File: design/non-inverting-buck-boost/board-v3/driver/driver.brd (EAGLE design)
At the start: 54.3 x 44.4 mm, 11 parts, among them IC1 L7812, IC2 78L05, T1 BC547

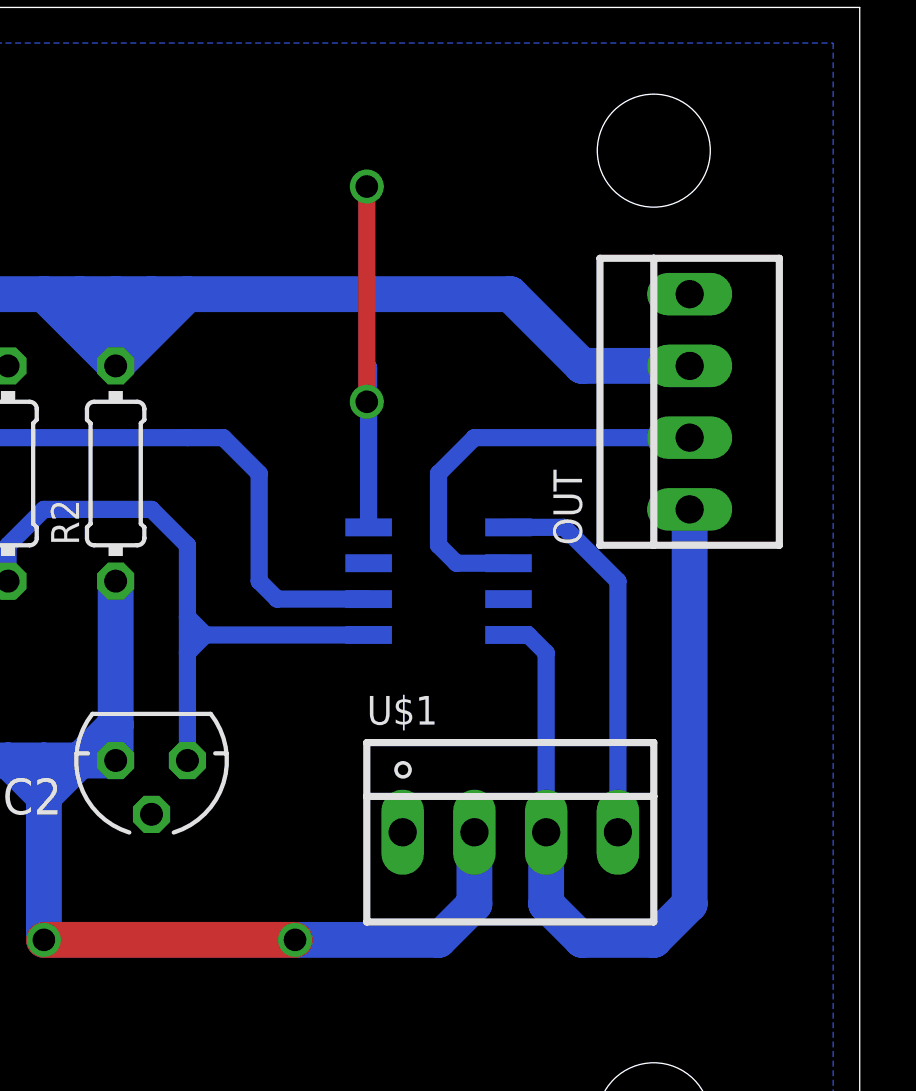
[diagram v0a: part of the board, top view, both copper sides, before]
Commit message: fixed ADuM3220 pins
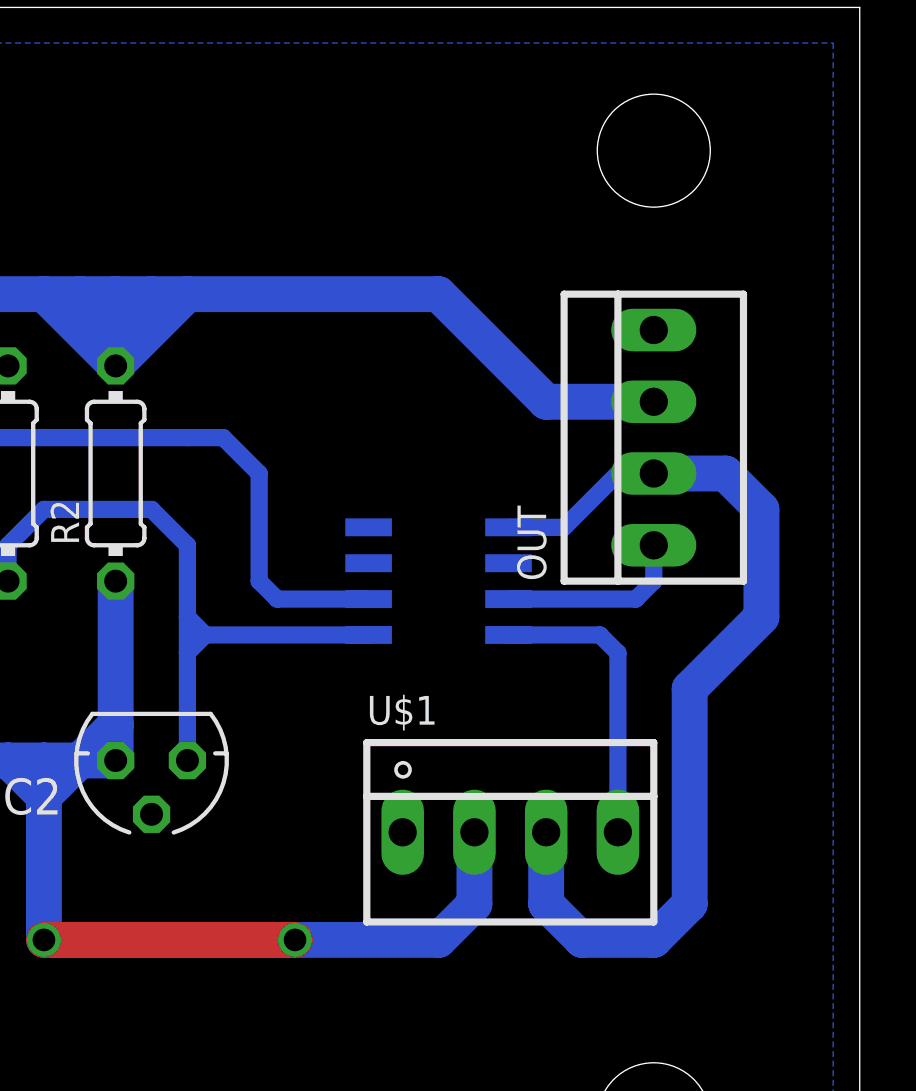
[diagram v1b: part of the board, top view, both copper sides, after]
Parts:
- moved OUT 1.80 mm to (47.0, 29.2)
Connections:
- net VDD2: now also U$2.8; no longer U$2.5
- net VG1: now also OUT.1, U$2.7; no longer OUT.2, U$2.6
- net VS1: now also OUT.2, U$2.5; no longer OUT.1, U$2.8
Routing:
- net GND: track 14.5 -> 0.00 mm, vias 2 -> 0
- net VG1: track 14.7 -> 6.68 mm
- net VS1: track 30.6 -> 34.0 mm
- net VDD2: track 13.6 -> 10.5 mm
- net VG2: track 46.6 -> 45.9 mm
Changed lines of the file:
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@@
 <attribute name="OC_NEWARK" value="25C3832" x="7.62" y="29.21" size="1.778" layer="27" rot="R270" display="off"/>
 </element>
-<element name="OUT" library="con-molex" package="22-23-2041" value="22-23-2041" x="48.26" y="30.48" rot="R90">
-<attribute name="MF" value="MOLEX" x="48.26" y="30.48" size="1.778" layer="27" rot="R90" display="off"/>
-<attribute name="MPN" value="22-23-2041" x="48.26" y="30.48" size="1.778" layer="27" rot="R90" display="off"/>
-<attribute name="OC_FARNELL" value="1462920" x="48.26" y="30.48" size="1.778" layer="27" rot="R90" display="off"/>
-<attribute name="OC_NEWARK" value="38C0355" x="48.26" y="30.48" size="1.778" layer="27" rot="R90" display="off"/>
+<element name="OUT" library="con-molex" package="22-23-2041" value="22-23-2041" x="46.99" y="29.21" rot="R90">
+<attribute name="MF" value="MOLEX" x="46.99" y="29.21" size="1.778" layer="27" rot="R90" display="off"/>
+<attribute name="MPN" value="22-23-2041" x="46.99" y="29.21" size="1.778" layer="27" rot="R90" display="off"/>
+<attribute name="OC_FARNELL" value="1462920" x="46.99" y="29.21" size="1.778" layer="27" rot="R90" display="off"/>
+<attribute name="OC_NEWARK" value="38C0355" x="46.99" y="29.21" size="1.778" layer="27" rot="R90" display="off"/>
 </element>
 <element name="T1" library="transistor" package="TO92" value="BC547" x="16.51" y="31.75" rot="R270"/>
@@
 <signal name="VDD2">
 <contactref element="U$1" pad="4"/>
-<contactref element="U$2" pad="5"/>
-<wire x1="41.8465" y1="26.035" x2="43.815" y2="26.035" width="0.6096" layer="16"/>
-<wire x1="43.815" y1="26.035" x2="45.72" y2="24.13" width="0.6096" layer="16"/>
-<wire x1="45.72" y1="24.13" x2="45.72" y2="15.24" width="0.6096" layer="16"/>
+<contactref element="U$2" pad="8"/>
+<wire x1="41.8465" y1="22.225" x2="45.085" y2="22.225" width="0.6096" layer="16"/>
+<wire x1="45.085" y1="22.225" x2="45.72" y2="21.59" width="0.6096" layer="16"/>
+<wire x1="45.72" y1="21.59" x2="45.72" y2="15.24" width="0.6096" layer="16"/>
 </signal>
 <signal name="VS1">
 <contactref element="U$1" pad="3"/>
-<contactref element="U$2" pad="8"/>
-<contactref element="OUT" pad="1"/>
-<wire x1="41.8465" y1="22.225" x2="42.545" y2="22.225" width="0.6096" layer="16"/>
-<wire x1="43.18" y1="21.59" x2="42.545" y2="22.225" width="0.6096" layer="16"/>
-<wire x1="43.18" y1="15.24" x2="43.18" y2="21.59" width="0.6096" layer="16"/>
-<wire x1="48.26" y1="26.67" x2="48.26" y2="12.7" width="1.27" layer="16"/>
+<contactref element="U$2" pad="5"/>
+<contactref element="OUT" pad="2"/>
+<wire x1="41.8465" y1="26.035" x2="43.815" y2="26.035" width="0.6096" layer="16"/>
+<wire x1="45.72" y1="27.94" x2="46.99" y2="27.94" width="0.6096" layer="16"/>
+<wire x1="43.815" y1="26.035" x2="45.72" y2="27.94" width="0.6096" layer="16"/>
+<wire x1="46.99" y1="27.94" x2="49.53" y2="27.94" width="1.27" layer="16"/>
+<wire x1="49.53" y1="27.94" x2="50.8" y2="26.67" width="1.27" layer="16"/>
+<wire x1="50.8" y1="26.67" x2="50.8" y2="22.86" width="1.27" layer="16"/>
+<wire x1="50.8" y1="22.86" x2="48.26" y2="20.32" width="1.27" layer="16"/>
+<wire x1="48.26" y1="20.32" x2="48.26" y2="12.7" width="1.27" layer="16"/>
 <wire x1="48.26" y1="12.7" x2="46.99" y2="11.43" width="1.27" layer="16"/>
 <wire x1="46.99" y1="11.43" x2="44.45" y2="11.43" width="1.27" layer="16"/>
@@
 <vertex x="53.34" y="1.27"/>
 </polygon>
-<wire x1="36.8935" y1="26.035" x2="36.8935" y2="31.6865" width="0.6096" layer="16"/>
-<wire x1="36.8935" y1="31.6865" x2="36.83" y2="30.48" width="0.6096" layer="16"/>
-<via x="36.83" y="30.48" extent="1-16" drill="0.8" shape="square"/>
-<wire x1="36.83" y1="30.48" x2="36.83" y2="38.1" width="0.6096" layer="1"/>
-<via x="36.83" y="38.1" extent="1-16" drill="0.8" shape="square"/>
 </signal>
 <signal name="N$6">
@@
 <wire x1="29.21" y1="34.29" x2="30.48" y2="34.29" width="1.27" layer="16"/>
 <wire x1="29.21" y1="34.29" x2="27.94" y2="34.29" width="1.27" layer="16"/>
-<wire x1="30.48" y1="34.29" x2="41.91" y2="34.29" width="1.27" layer="16"/>
-<wire x1="41.91" y1="34.29" x2="44.45" y2="31.75" width="1.27" layer="16"/>
-<wire x1="44.45" y1="31.75" x2="48.26" y2="31.75" width="1.27" layer="16"/>
 <wire x1="27.94" y1="34.29" x2="27.94" y2="33.02" width="1.27" layer="16"/>
 <wire x1="27.94" y1="33.02" x2="27.94" y2="31.75" width="1.27" layer="16"/>
@@
 <wire x1="27.94" y1="33.02" x2="26.67" y2="34.29" width="1.27" layer="16"/>
 <wire x1="27.94" y1="33.02" x2="29.21" y2="34.29" width="1.27" layer="16"/>
+<wire x1="30.48" y1="34.29" x2="39.37" y2="34.29" width="1.27" layer="16"/>
+<wire x1="39.37" y1="34.29" x2="43.18" y2="30.48" width="1.27" layer="16"/>
+<wire x1="43.18" y1="30.48" x2="46.99" y2="30.48" width="1.27" layer="16"/>
 </signal>
 <signal name="N$4">
@@
 </signal>
 <signal name="VG1">
-<contactref element="OUT" pad="2"/>
-<contactref element="U$2" pad="6"/>
-<wire x1="41.8465" y1="24.765" x2="40.005" y2="24.765" width="0.6096" layer="16"/>
-<wire x1="40.005" y1="24.765" x2="39.37" y2="25.4" width="0.6096" layer="16"/>
-<wire x1="39.37" y1="25.4" x2="39.37" y2="27.94" width="0.6096" layer="16"/>
-<wire x1="39.37" y1="27.94" x2="40.64" y2="29.21" width="0.6096" layer="16"/>
-<wire x1="40.64" y1="29.21" x2="48.26" y2="29.21" width="0.6096" layer="16"/>
+<contactref element="OUT" pad="1"/>
+<contactref element="U$2" pad="7"/>
+<wire x1="41.8465" y1="23.495" x2="46.355" y2="23.495" width="0.6096" layer="16"/>
+<wire x1="46.355" y1="23.495" x2="46.99" y2="24.13" width="0.6096" layer="16"/>
+<wire x1="46.99" y1="24.13" x2="46.99" y2="25.4" width="0.6096" layer="16"/>
 </signal>
 </signals>
